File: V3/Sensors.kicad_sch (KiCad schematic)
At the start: 16 parts, among them U1 L80-M39, U10 BMX055, U2 MS561101BA03-50, U3 ADXL375BCCZ-RL7

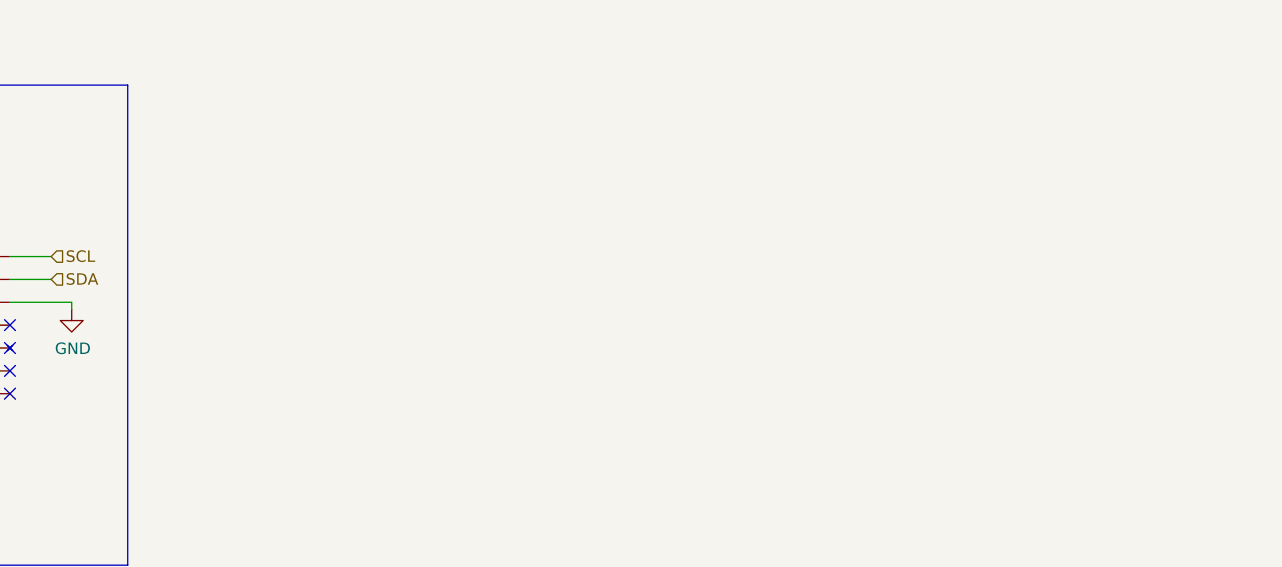
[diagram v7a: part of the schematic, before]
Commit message: Added reccomended changes for V3
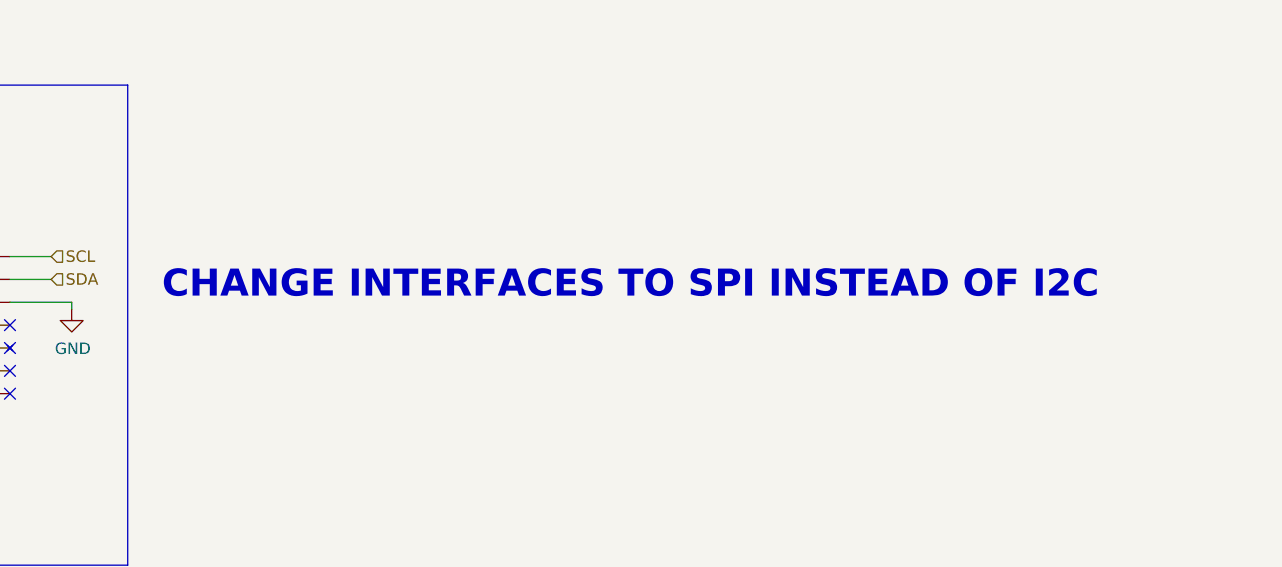
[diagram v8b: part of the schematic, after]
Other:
- note added: "CHANGE INTERFACES TO SPI INSTEAD OF I2C"
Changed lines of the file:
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@@
     (effects (font (size 3.9878 3.9878)) (justify left bottom))
+  )
+  (text "CHANGE INTERFACES TO SPI INSTEAD OF I2C" (at 234.188 47.498 0)
+    (effects (font (size 3 3) (thickness 0.6) bold) (justify left bottom))
   )
   (text "GPS - L80 M39  " (at 71.755 22.225 0)
